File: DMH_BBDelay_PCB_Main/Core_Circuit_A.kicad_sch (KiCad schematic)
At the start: 59 parts, among them Q3 J113, SW3 SW_SPDT, U1 TL074, U2 TL074, U3 V3205, U4 CD4046

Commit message: Implemented Link switch in schematic
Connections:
- net at C16.2: now also SW3.3 (C); no longer SW3.1 (A)
- net Clock_A_m: now reaches C14.1, U3.6 (CP1), U4.3 (RefIn), U4.4 (FOUT)
- net at C15.2: now also SW3.1 (A); no longer SW3.3 (C)
- net VCXF_DW_A/In_A renamed D_A_m
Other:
- moved on the sheet: C15, C16
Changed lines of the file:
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@@
 	)
 	(junction
+		(at 292.1 15.24)
+		(diameter 0)
+		(color 0 0 0 0)
+	)
+	(junction
 		(at 107.95 54.61)
 		(diameter 0)
@@
 	(wire
 		(pts
+			(xy 127 120.65) (xy 133.35 120.65)
+		)
+		(stroke
+			(width 0)
+			(type default)
+		)
+	)
+	(wire
+		(pts
 			(xy 245.11 149.86) (xy 250.19 149.86)
 		)
@@
 	(wire
 		(pts
+			(xy 292.1 15.24) (xy 294.64 15.24)
+		)
+		(stroke
+			(width 0)
+			(type default)
+		)
+	)
+	(wire
+		(pts
 			(xy 127 173.99) (xy 127 157.48)
 		)
@@
 		)
 	)
+	(global_label "D_A_m"
+		(shape output)
+		(at 294.64 15.24 0)
+		(fields_autoplaced yes)
+		(effects
+			(font
+				(size 1.27 1.27)
+			)
+			(justify left)
+		)
+		(property "Intersheetrefs" "${INTERSHEET_REFS}"
+			(at 303.6123 15.24 0)
+			(hide yes)
+			(show_name no)
+			(do_not_autoplace no)
+			(effects
+				(font
+					(size 1.27 1.27)
+				)
+				(justify left)
+			)
+		)
+	)
 	(global_label "A_In_m"
 		(shape input)
@@
 		)
 	)
+	(global_label "Clock_A_m"
+		(shape output)
+		(at 127 120.65 180)
+		(fields_autoplaced yes)
+		(effects
+			(font
+				(size 1.27 1.27)
+			)
+			(justify right)
+		)
+		(property "Intersheetrefs" "${INTERSHEET_REFS}"
+			(at 114.0968 120.65 0)
+			(hide yes)
+			(show_name no)
+			(do_not_autoplace no)
+			(effects
+				(font
+					(size 1.27 1.27)
+				)
+				(justify right)
+			)
+		)
+	)
 	(global_label "DW_A_CV_Pot_c"
 		(shape output)
@@
 	(symbol
 		(lib_id "Device:C")
-		(at 82.55 153.67 90)
+		(at 82.55 142.24 90)
 		(unit 1)
 		(body_style 1)
@@
 		(dnp no)
 		(property "Reference" "C16"
-			(at 82.55 147.066 90)
+			(at 82.55 135.636 90)
 			(show_name no)
 			(do_not_autoplace no)
@@
 		)
 		(property "Value" "1nF"
-			(at 82.55 149.606 90)
+			(at 82.55 138.176 90)
 			(show_name no)
 			(do_not_autoplace no)
@@
 		)
 		(property "Footprint" "Capacitor_THT:C_Disc_D3.0mm_W2.0mm_P2.50mm"
-			(at 86.36 152.7048 0)
+			(at 86.36 141.2748 0)
 			(hide yes)
 			(show_name no)
@@
 		)
 		(property "Datasheet" ""
-			(at 82.55 153.67 0)
+			(at 82.55 142.24 0)
 			(hide yes)
 			(show_name no)
@@
 		)
 		(property "Description" "Unpolarized capacitor"
-			(at 82.55 153.67 0)
+			(at 82.55 142.24 0)
 			(hide yes)
 			(show_name no)
@@
 		)
 		(property "Function" ""
-			(at 82.55 153.67 0)
+			(at 82.55 142.24 0)
 			(show_name no)
 			(do_not_autoplace no)
@@
 	(symbol
 		(lib_id "Device:C")
-		(at 82.55 142.24 90)
+		(at 82.55 153.67 90)
 		(unit 1)
 		(body_style 1)
@@
 		(dnp no)
 		(property "Reference" "C15"
-			(at 82.55 135.636 90)
+			(at 82.55 147.066 90)
 			(show_name no)
 			(do_not_autoplace no)
@@
 		)
 		(property "Value" "220pF"
-			(at 82.55 138.176 90)
+			(at 82.55 149.606 90)
 			(show_name no)
 			(do_not_autoplace no)
@@
 		)
 		(property "Footprint" "Capacitor_THT:C_Disc_D3.0mm_W2.0mm_P2.50mm"
-			(at 86.36 141.2748 0)
+			(at 86.36 152.7048 0)
 			(hide yes)
 			(show_name no)
@@
 		)
 		(property "Datasheet" ""
-			(at 82.55 142.24 0)
+			(at 82.55 153.67 0)
 			(hide yes)
 			(show_name no)
@@
 		)
 		(property "Description" "Unpolarized capacitor"
-			(at 82.55 142.24 0)
+			(at 82.55 153.67 0)
 			(hide yes)
 			(show_name no)
@@
 		)
 		(property "Function" ""
-			(at 82.55 142.24 0)
+			(at 82.55 153.67 0)
 			(show_name no)
 			(do_not_autoplace no)

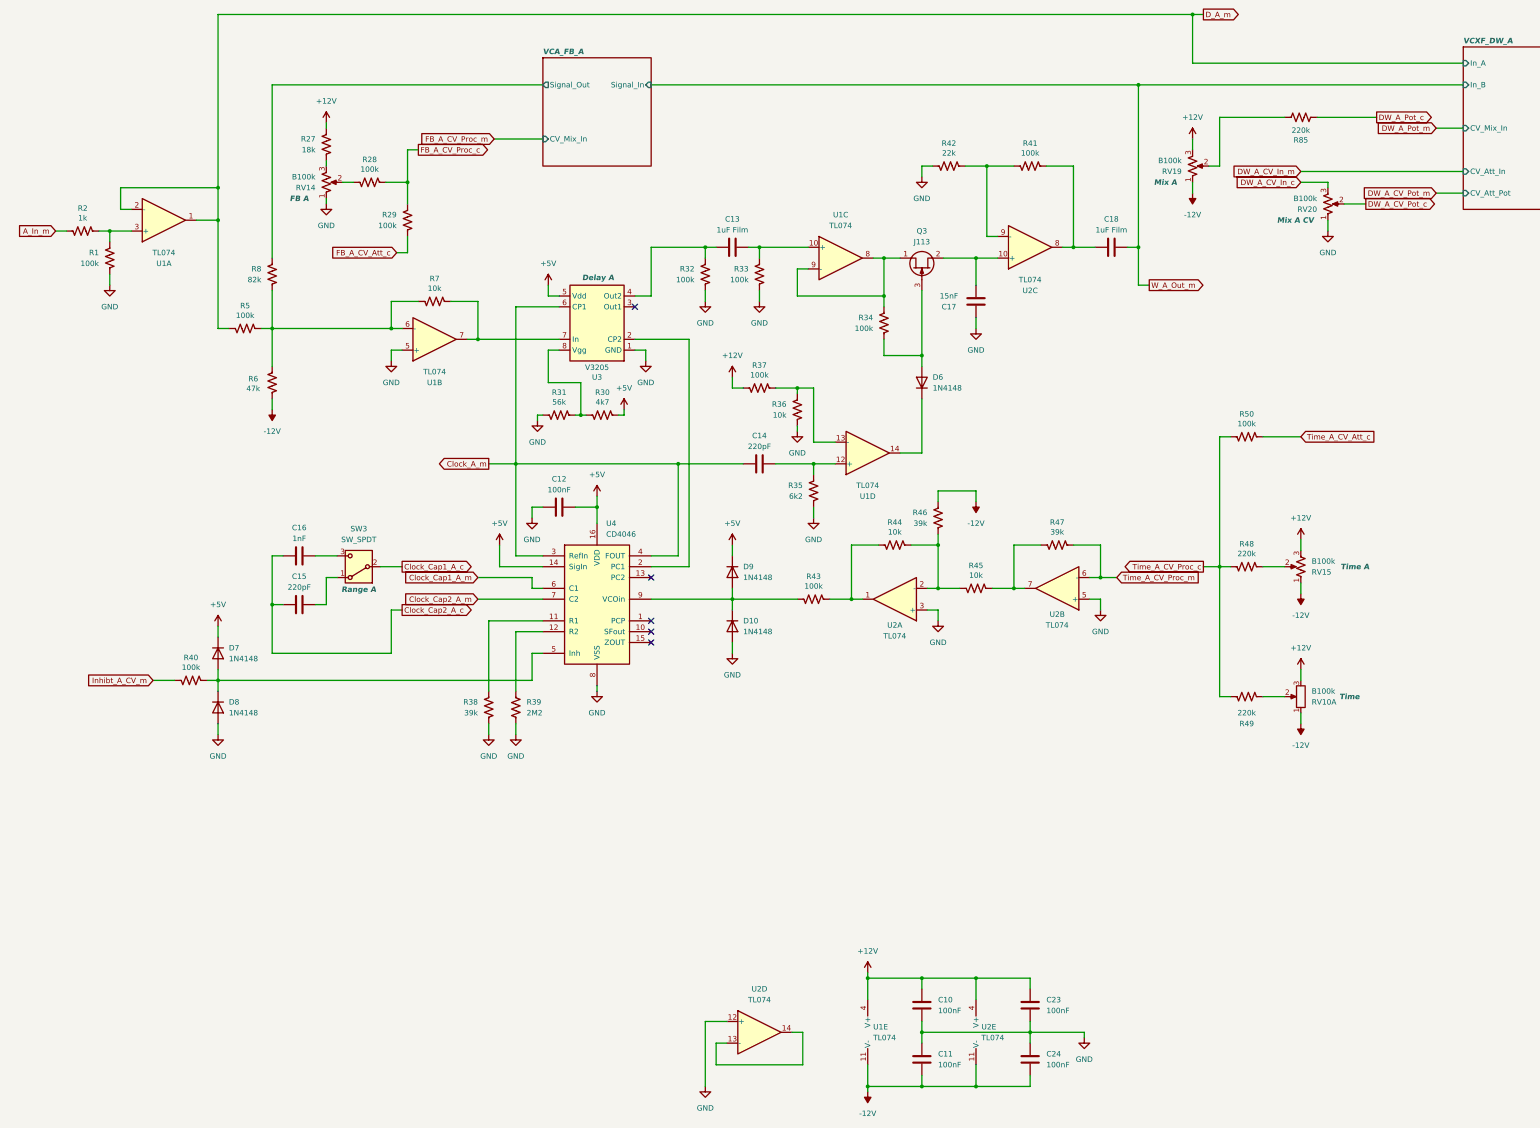
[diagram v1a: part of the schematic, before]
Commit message: Schematic in progress
Added AC coupling to inputs
Buffered wet outputs
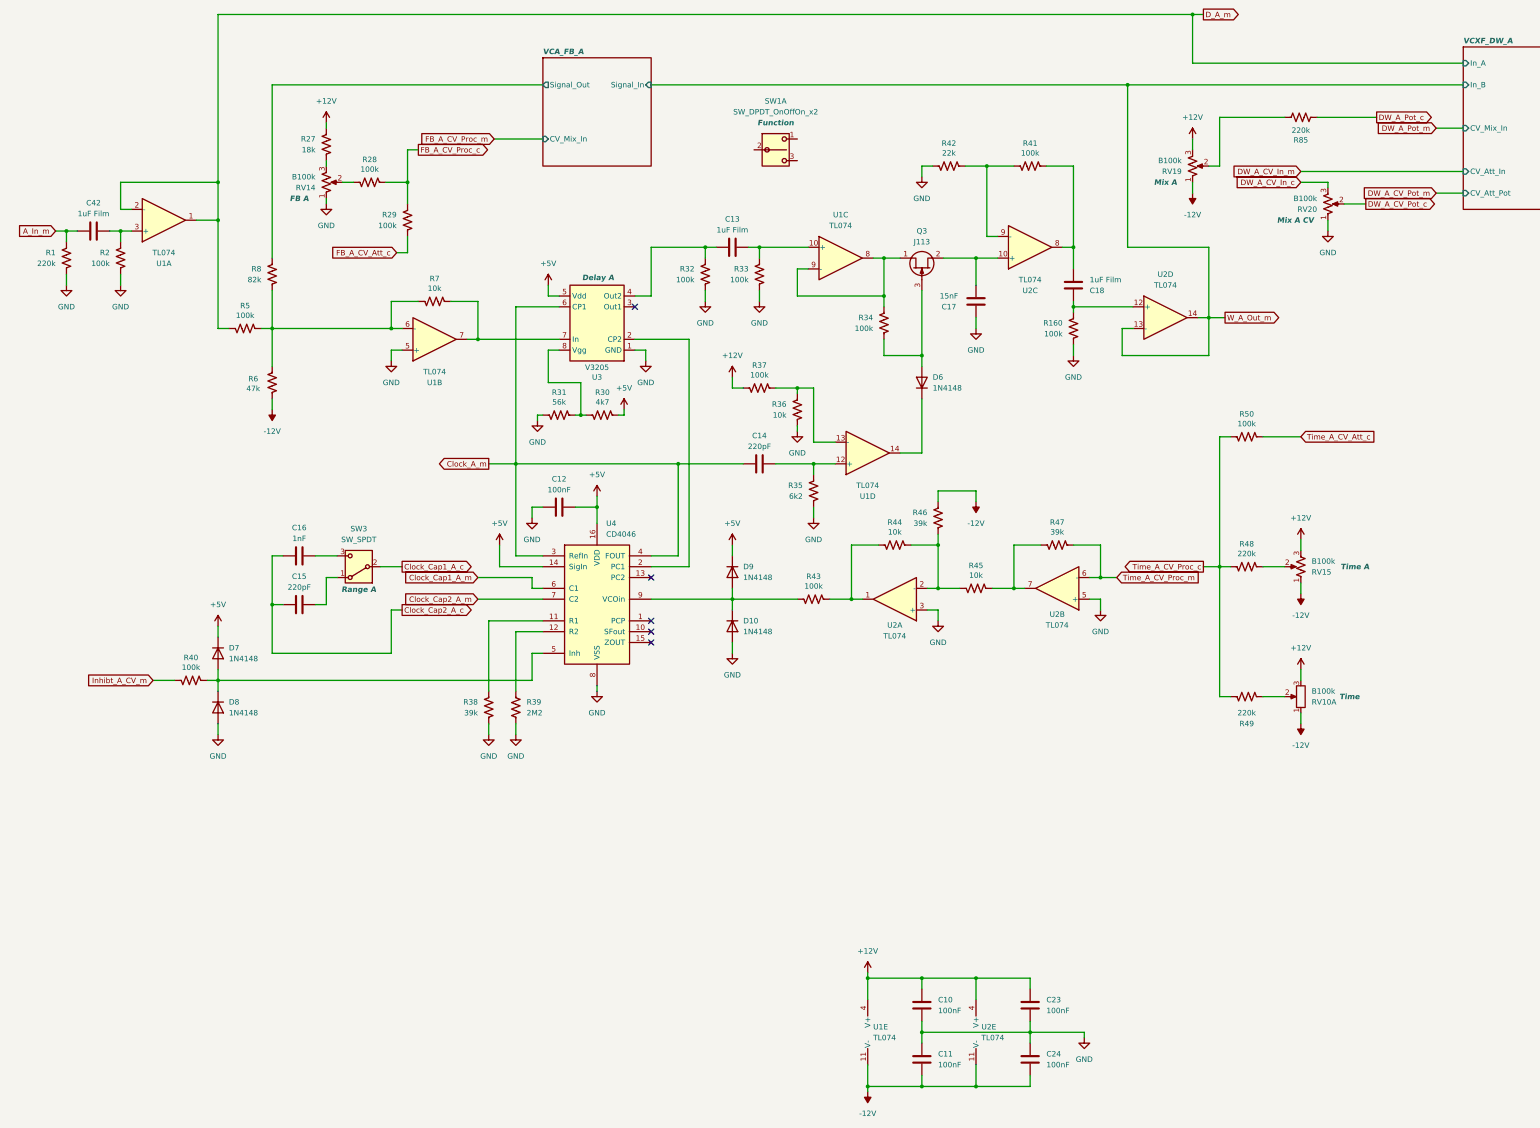
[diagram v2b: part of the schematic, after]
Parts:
- removed R2: 1k, Resistor_THT:R_Axial_DIN0207_L6.3mm_D2.5mm_P7.62mm_Horizontal, symbol Device:R_US
- added C42: 1uF Film, Capacitor_THT:C_Disc_D7.5mm_W5.0mm_P5.00mm, symbol Device:C
- added R1: 220k, Resistor_THT:R_Axial_DIN0207_L6.3mm_D2.5mm_P7.62mm_Horizontal, symbol Device:R_US
- added R160: 100k, Resistor_THT:R_Axial_DIN0207_L6.3mm_D2.5mm_P7.62mm_Horizontal, symbol Device:R_US
- added SW1: SW_DPDT_OnOffOn_x2, SynthStuff:Toggle_Switch_2_Poles_TE, symbol SynthStuff:SW_DPDT_OnOffOn_x2
- C13, C18: footprint Capacitor_THT:C_Disc_D7.5mm_W4.4mm_P5.00mm -> Capacitor_THT:C_Disc_D7.5mm_W5.0mm_P5.00mm
- renumbered R1 to R2
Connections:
- net A_In_m: now also C42.1, R1.2
- net GND: now also R1.1, R160.1; no longer U2.12 (+)
- net W_A_Out_m: now also U2.13 (-), U2.14; no longer C18.2
- net at R2.2, U1.3 (+): now also C42.2
- net at R41.2, U2.8: now also C18.2; no longer C18.1
- new net: C18.1, R160.2, U2.12 (+)
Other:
- moved on the sheet: C18, R2, U2D

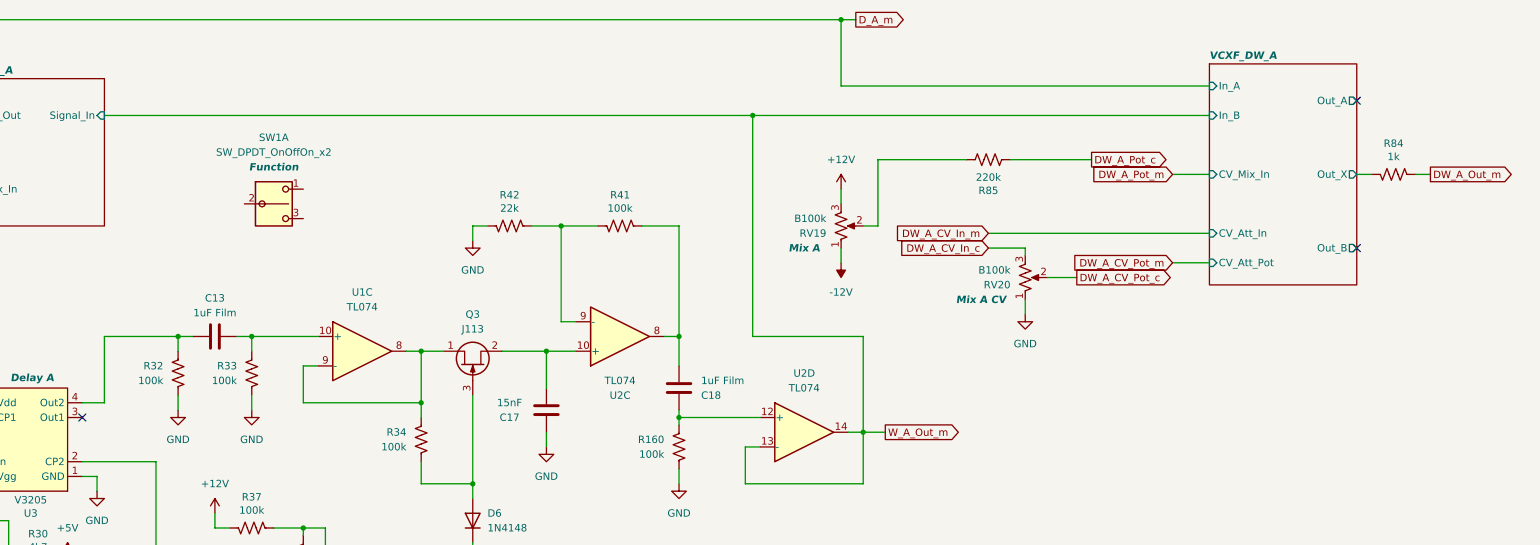
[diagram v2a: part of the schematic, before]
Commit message: Implemented Ping Pong funtion
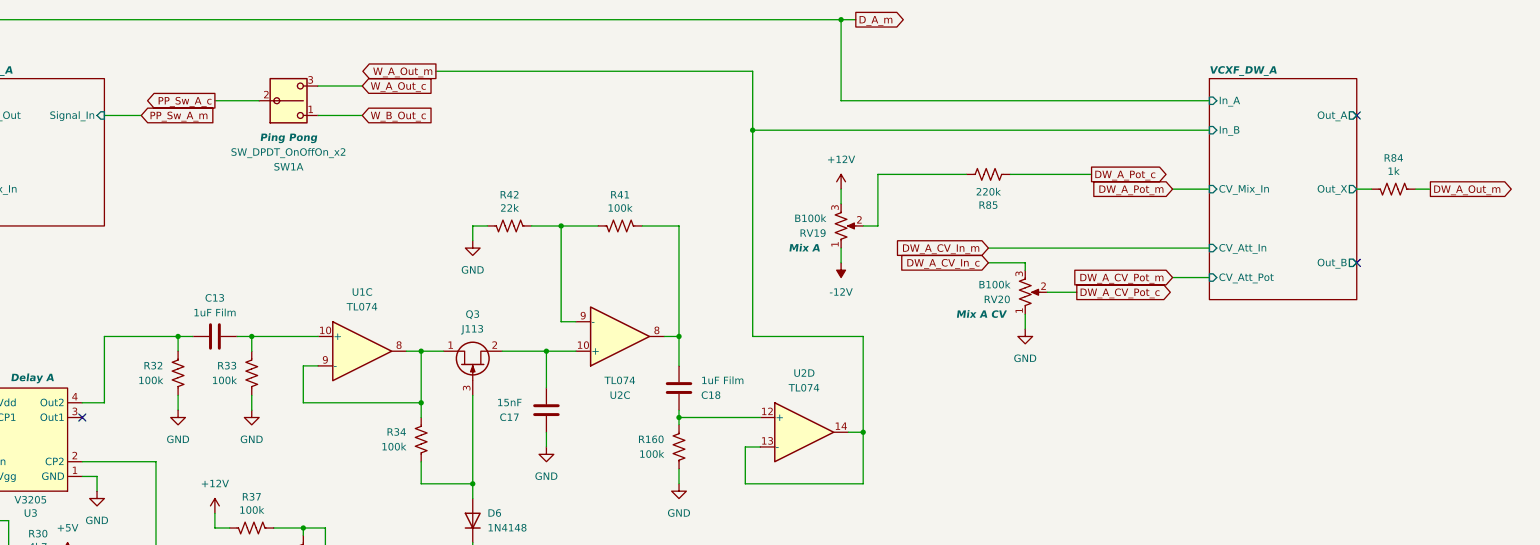
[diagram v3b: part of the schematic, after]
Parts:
- SW1: Function Function -> Ping Pong
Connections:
- net W_B_Out_c: now reaches SW1.1 (A)
- net PP_Sw_A_c: now reaches SW1.2 (B)
- net W_A_Out_c: now reaches SW1.3 (C)
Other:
- moved on the sheet: R84, R85, RV20, SW1A
